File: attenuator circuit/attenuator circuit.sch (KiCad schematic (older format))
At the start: 6 parts, among them J1 SJ1-3525N, J2 SJ1-3525N

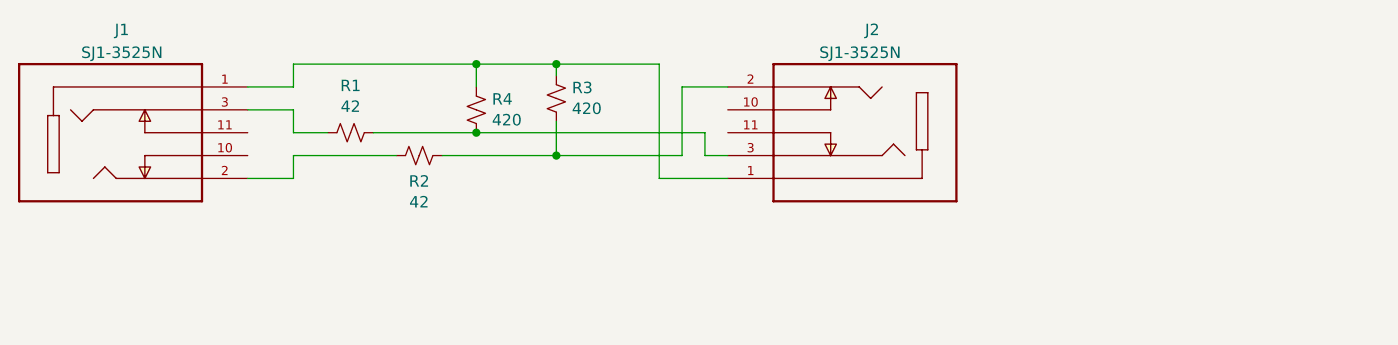
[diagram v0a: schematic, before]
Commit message: Version 2 of PCB
- re-arrange things to be more uniform
- shorten it slightly (Save $0.25! )
- widen the trace size
- makes use of a ground plane
- add some fancy labels
- label the resistors with actual values for most common scenario
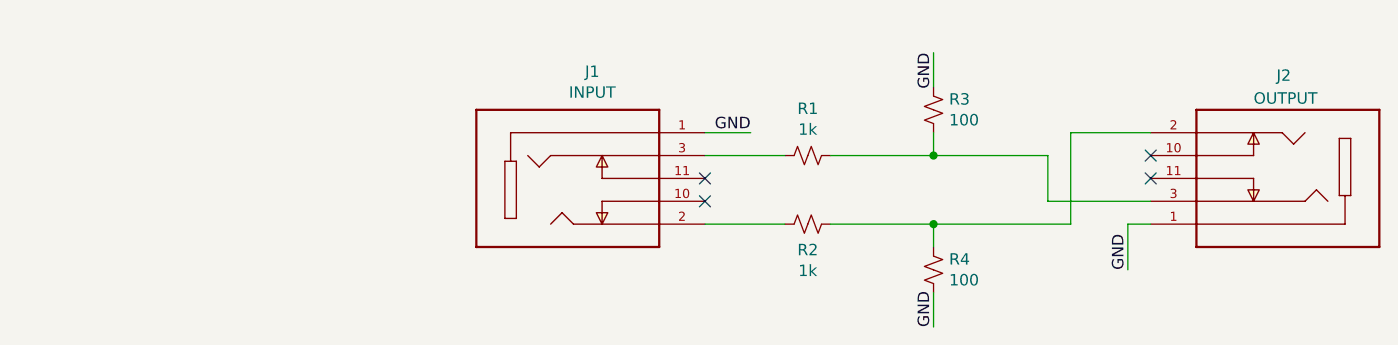
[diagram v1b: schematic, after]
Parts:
- J1: value SJ1-3525N -> INPUT
- J2: value SJ1-3525N -> OUTPUT
- R1, R2: value 42 -> 1k
- R3: renamed from R4; value 420 -> 100
- R4: renamed from R3; value 420 -> 100
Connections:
- net GND: now reaches J1.1, J2.1, R3.1
- net GND: now also R4.2; no longer R4.1
- net at J2.2, R2.1: now also R4.1; no longer R4.2
- no-connect marks 0 -> 4
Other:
- moved on the sheet: J1, J2, R1, R2, R3, R4
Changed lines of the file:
@@
 EELAYER 30 0
 EELAYER END
-$Descr A4 11693 8268
+$Descr A 11000 8500
 encoding utf-8
 Sheet 1 1
-Title ""
+Title "Audio Attenuator"
 Date ""
-Rev ""
+Rev "2"
 Comp ""
 Comment1 ""
 Comment2 ""
-Comment3 ""
-Comment4 ""
+Comment3 " "
+Comment4 "https://github.com/vrillusions/audio-attenuator-pcb"
 $EndDescr
 $Comp
 L Device:R_Small_US R1
 U 1 1 6114FDBF
-P 3350 3500
-F 0 "R1" V 3145 3500 50  0000 C CNN
-F 1 "42" V 3236 3500 50  0000 C CNN
-F 2 "Resistor_THT:R_Axial_DIN0207_L6.3mm_D2.5mm_P7.62mm_Horizontal" H 3350 3500 50  0001 C CNN
-F 3 "~" H 3350 3500 50  0001 C CNN
-	1    3350 3500
+P 5350 3600
+F 0 "R1" V 5145 3600 50  0000 C CNN
+F 1 "1k" V 5236 3600 50  0000 C CNN
+F 2 "Resistor_THT:R_Axial_DIN0207_L6.3mm_D2.5mm_P7.62mm_Horizontal" H 5350 3600 50  0001 C CNN
+F 3 "~" H 5350 3600 50  0001 C CNN
+	1    5350 3600
 	0    1    1    0
 $EndComp
@@
 L Device:R_Small_US R2
 U 1 1 61151C01
-P 3650 3600
-F 0 "R2" V 3763 3600 50  0000 C CNN
-F 1 "42" V 3854 3600 50  0000 C CNN
-F 2 "Resistor_THT:R_Axial_DIN0207_L6.3mm_D2.5mm_P7.62mm_Horizontal" H 3650 3600 50  0001 C CNN
-F 3 "~" H 3650 3600 50  0001 C CNN
-	1    3650 3600
+P 5350 3900
+F 0 "R2" V 5463 3900 50  0000 C CNN
+F 1 "1k" V 5554 3900 50  0000 C CNN
+F 2 "Resistor_THT:R_Axial_DIN0207_L6.3mm_D2.5mm_P7.62mm_Horizontal" H 5350 3900 50  0001 C CNN
+F 3 "~" H 5350 3900 50  0001 C CNN
+	1    5350 3900
 	0    1    1    0
 $EndComp
 $Comp
+L SJ1-3525N:SJ1-3525N J1
+U 1 1 61342E5F
+P 4300 3700
+F 0 "J1" H 4407 4167 50  0000 C CNN
+F 1 "INPUT" H 4407 4076 50  0000 C CNN
+F 2 "SJ1-3525N:CUI_SJ1-3525N" H 4300 3700 50  0001 L BNN
+F 3 "" H 4300 3700 50  0001 L BNN
+F 4 "1.02" H 4300 3700 50  0001 L BNN "PARTREV"
+F 5 "Manufacturer recommendation" H 4300 3700 50  0001 L BNN "STANDARD"
+F 6 "CUI" H 4300 3700 50  0001 L BNN "MANUFACTURER"
+	1    4300 3700
+	1    0    0    -1
+$EndComp
+$Comp
+L SJ1-3525N:SJ1-3525N J2
+U 1 1 61347F3C
+P 7450 3700
+F 0 "J2" H 7500 3250 50  0000 R CNN
+F 1 "OUTPUT" H 7600 3350 50  0000 R CNN
+F 2 "SJ1-3525N:CUI_SJ1-3525N" H 7450 3700 50  0001 L BNN
+F 3 "" H 7450 3700 50  0001 L BNN
+F 4 "1.02" H 7450 3700 50  0001 L BNN "PARTREV"
+F 5 "Manufacturer recommendation" H 7450 3700 50  0001 L BNN "STANDARD"
+F 6 "CUI" H 7450 3700 50  0001 L BNN "MANUFACTURER"
+	1    7450 3700
+	-1   0    0    1
+$EndComp
+Wire Wire Line
+	4900 3500 5100 3500
+Text Label 5100 3500 2    50   ~ 0
+GND
+Text Label 5900 3150 3    50   ~ 0
+GND
+Wire Wire Line
+	5900 4000 5900 3900
+Wire Wire Line
+	5900 4200 5900 4350
+Text Label 5900 4350 1    50   ~ 0
+GND
+Wire Wire Line
+	6850 3900 6750 3900
+Wire Wire Line
+	6750 3900 6750 4100
+Text Label 6750 4100 1    50   ~ 0
+GND
+NoConn ~ 4900 3700
+NoConn ~ 4900 3800
+NoConn ~ 6850 3600
+NoConn ~ 6850 3700
+$Comp
 L Device:R_Small_US R4
-U 1 1 611522E0
-P 3900 3400
-F 0 "R4" H 3968 3446 50  0000 L CNN
-F 1 "420" H 3968 3355 50  0000 L CNN
-F 2 "Resistor_THT:R_Axial_DIN0207_L6.3mm_D2.5mm_P7.62mm_Horizontal" H 3900 3400 50  0001 C CNN
-F 3 "~" H 3900 3400 50  0001 C CNN
-	1    3900 3400
+U 1 1 61150F26
+P 5900 4100
+F 0 "R4" H 5968 4146 50  0000 L CNN
+F 1 "100" H 5968 4055 50  0000 L CNN
+F 2 "Resistor_THT:R_Axial_DIN0207_L6.3mm_D2.5mm_P7.62mm_Horizontal" H 5900 4100 50  0001 C CNN
+F 3 "~" H 5900 4100 50  0001 C CNN
+	1    5900 4100
 	1    0    0    -1
 $EndComp
 Wire Wire Line
-	3100 3600 3550 3600
+	4900 3900 5250 3900
 Wire Wire Line
-	3450 3500 3900 3500
+	6500 3900 6500 3500
 Wire Wire Line
-	3100 3200 3900 3200
+	6500 3500 6850 3500
 Wire Wire Line
-	3900 3200 3900 3300
-Connection ~ 3900 3200
+	4900 3600 5250 3600
+Wire Wire Line
+	6400 3600 6400 3800
+Wire Wire Line
+	6850 3800 6400 3800
+Wire Wire Line
+	5450 3600 5900 3600
+Wire Wire Line
+	5450 3900 5900 3900
+Wire Wire Line
+	5900 3900 6500 3900
+Connection ~ 5900 3900
+Wire Wire Line
+	5900 3600 6400 3600
+Connection ~ 5900 3600
 $Comp
 L Device:R_Small_US R3
-U 1 1 61150F26
-P 4250 3350
-F 0 "R3" H 4318 3396 50  0000 L CNN
-F 1 "420" H 4318 3305 50  0000 L CNN
-F 2 "Resistor_THT:R_Axial_DIN0207_L6.3mm_D2.5mm_P7.62mm_Horizontal" H 4250 3350 50  0001 C CNN
-F 3 "~" H 4250 3350 50  0001 C CNN
-	1    4250 3350
+U 1 1 611522E0
+P 5900 3400
+F 0 "R3" H 5968 3446 50  0000 L CNN
+F 1 "100" H 5968 3355 50  0000 L CNN
+F 2 "Resistor_THT:R_Axial_DIN0207_L6.3mm_D2.5mm_P7.62mm_Horizontal" H 5900 3400 50  0001 C CNN
+F 3 "~" H 5900 3400 50  0001 C CNN
+	1    5900 3400
 	1    0    0    -1
 $EndComp
 Wire Wire Line
-	3900 3200 4250 3200
+	5900 3300 5900 3150
 Wire Wire Line
-	4250 3200 4250 3250
-Wire Wire Line
-	3750 3600 4250 3600
-Connection ~ 4250 3200
-Wire Wire Line
-	4250 3200 4700 3200
-Wire Wire Line
-	4250 3450 4250 3600
-Connection ~ 4250 3600
-$Comp
-L SJ1-3525N:SJ1-3525N J1
-U 1 1 61342E5F
-P 2300 3500
-F 0 "J1" H 2350 3950 50  0000 C CNN
-F 1 "SJ1-3525N" H 2350 3850 50  0000 C CNN
-F 2 "SJ1-3525N:CUI_SJ1-3525N" H 2300 3500 50  0001 L BNN
-F 3 "" H 2300 3500 50  0001 L BNN
-F 4 "1.02" H 2300 3500 50  0001 L BNN "PARTREV"
-F 5 "Manufacturer recommendation" H 2300 3500 50  0001 L BNN "STANDARD"
-F 6 "CUI" H 2300 3500 50  0001 L BNN "MANUFACTURER"
-	1    2300 3500
-	1    0    0    -1
-$EndComp
-Wire Wire Line
-	3100 3500 3250 3500
-Wire Wire Line
-	2900 3400 3100 3400
-Wire Wire Line
-	3100 3400 3100 3500
-Wire Wire Line
-	2900 3700 3100 3700
-Wire Wire Line
-	3100 3700 3100 3600
-Wire Wire Line
-	2900 3300 3100 3300
-Wire Wire Line
-	3100 3300 3100 3200
-$Comp
-L SJ1-3525N:SJ1-3525N J2
-U 1 1 61347F3C
-P 5600 3500
-F 0 "J2" H 5600 3050 50  0000 R CNN
-F 1 "SJ1-3525N" H 5800 3150 50  0000 R CNN
-F 2 "SJ1-3525N:CUI_SJ1-3525N" H 5600 3500 50  0001 L BNN
-F 3 "" H 5600 3500 50  0001 L BNN
-F 4 "1.02" H 5600 3500 50  0001 L BNN "PARTREV"
-F 5 "Manufacturer recommendation" H 5600 3500 50  0001 L BNN "STANDARD"
-F 6 "CUI" H 5600 3500 50  0001 L BNN "MANUFACTURER"
-	1    5600 3500
-	-1   0    0    1
-$EndComp
-Wire Wire Line
-	4700 3200 4700 3700
-Wire Wire Line
-	4700 3700 5000 3700
-Wire Wire Line
-	4800 3600 4800 3300
-Wire Wire Line
-	4800 3300 5000 3300
-Wire Wire Line
-	4250 3600 4800 3600
-Wire Wire Line
-	3900 3500 4900 3500
-Wire Wire Line
-	4900 3500 4900 3600
-Wire Wire Line
-	4900 3600 5000 3600
-Connection ~ 3900 3500
+	5900 3600 5900 3500
 $EndSCHEMATC
